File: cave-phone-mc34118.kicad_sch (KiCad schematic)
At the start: 53 parts

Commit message: v0.1 (wrong U2 package)
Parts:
- removed SW?: SW_SPST, symbol Switch:SW_SPST
- added BT1: 18650, Battery:BatteryHolder_MPD_BH-18650-PC2, symbol Device:Battery_Cell
- added C1: 4,7µF, Capacitor_Tantalum_SMD:CP_EIA-3528-21_Kemet-B, symbol Device:C_Polarized
- added C12: 150pF, Capacitor_SMD:C_0603_1608Metric, symbol Device:C
- added C16: 20µF, Capacitor_Tantalum_SMD:CP_EIA-3528-21_Kemet-B, symbol Device:C_Polarized
- added C29: 1000µF, Capacitor_SMD:CP_Elec_10x10.5, symbol Device:C_Polarized
- added D1: BAT760.115, Diode_SMD:D_SOD-323, symbol Device:D_Schottky
- added D2: DB107GS, Diode_SMD:Diode_Bridge_Vishay_DFS, symbol Device:D_Bridge_+-AA
- added D3: BZV55C5V1, Diode_SMD:D_MiniMELF, symbol Diode:BZV55C5V1
- added D4: PESD5V0L1BA, Diode_SMD:D_SOD-323, symbol cave-phone:PESD5V0L1BA
- added D5: LED, LED_THT:LED_D3.0mm, symbol Device:LED
- added E1: 2051-09-SM-RPLF (90V), Fuse:Fuse_1812_4532Metric, symbol Device:SparkGap
- added J1: Conn_01x02_Female, Connector_Molex:Molex_SPOX_5267-02A_1x02_P2.50mm_Vertical, symbol Connector:Conn_01x02_Female
- added L1: 1,8µH, Inductor_SMD:L_1008_2520Metric, symbol Device:L
- added R23: 5K, Resistor_SMD:R_0603_1608Metric, symbol Device:R
- added R8: 29,4K, Resistor_SMD:R_0603_1608Metric, symbol Device:R
- added R9: 10K, Resistor_SMD:R_0603_1608Metric, symbol Device:R
- added SW1: L-KLS7-SK02-12E12-EG7, cave-phone:KLS7-SK02-12E12, symbol Switch:SW_SPDT
- added SW3: SW_SPST, Connector_PinHeader_2.54mm:PinHeader_1x02_P2.54mm_Vertical, symbol Switch:SW_SPST
- added U1: LT1935, Package_TO_SOT_SMD:SOT-23-5, symbol cave-phone:LT1935
- C10, C11, C13, C14, C15, C17, C18, C19, C20, C21, C22, C23, C24, C26, C27, C28, C4, C6, C7, C9: renamed from C?; footprint (none) -> Capacitor_SMD:C_0603_1608Metric
- C2, C25, C8: renamed from C?; footprint (none) -> Capacitor_Tantalum_SMD:CP_EIA-3528-21_Kemet-B
- C3: renamed from C?; footprint (none) -> Capacitor_Tantalum_SMD:CP_EIA-3528-21_Kemet-B; symbol Device:C -> Device:C_Polarized
- C5: renamed from C?; footprint (none) -> Capacitor_SMD:C_0805_2012Metric
- LS1: renamed from LS?; footprint (none) -> Connector_Molex:Molex_SPOX_5267-02A_1x02_P2.50mm_Vertical
- MK1: renamed from MK?; footprint (none) -> snapeda-mic:MIC_CMA-4544PF-W
- R1, R10, R11, R12, R13, R14, R15, R16, R17, R18, R19, R2, R20, R21, R22, R3, R4, R5, R6, R7: renamed from R?; footprint (none) -> Resistor_SMD:R_0603_1608Metric
- RV1: renamed from RV?; footprint (none) -> Potentiometer_THT:Potentiometer_Alps_RK163_Single_Horizontal
- SW2: renamed from SW?; footprint (none) -> Button_Switch_SMD:SW_Push_1P1T_NO_6x6mm_H9.5mm
- T1: renamed from T?; value Transformer_1P_1S -> SM-LP-5001; footprint (none) -> cave-phone:SM-LP-5001
- U2: renamed from U?; footprint Package_SO:SSOP-28_5.3x10.2mm_P0.65mm -> Package_SO:SOIC-28W_7.5x17.9mm_P1.27mm
- U3: renamed from U?; value MC34119P -> MC34119G-SO8; footprint Package_DIP:DIP-8_W7.62mm -> Package_SO:SOP-8_3.9x4.9mm_P1.27mm; symbol cave-phone:MC34119P -> cave-phone:MC34119G-S08-R
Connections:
- net GND: now also C3.2, U2.3 (CD), U3.1 (CD), BT1.2 (-), C1.2, C16.2, C29.2, D2.2 (-), D3.2 (A), R23.2, R9.2, U1.2 (GND); no longer C3.1
- net VCC: now also C12.2, C16.1, C29.1, D1.1 (K), D2.1 (+), D3.1 (K), D5.2 (A), R8.1
- net at R1.2, U2.14 (CT): now also C3.1; no longer C3.2
- net at T1.3 (SA): now also D2.4, SW3.1 (A)
- net at T1.4 (SB): now also D4.2 (A), E1.2, J1.1 (Pin_1)
- new net: C1.1, L1.1, SW1.3 (C), U1.4 (EN), U1.5 (VIN)
- new net: D1.2 (A), L1.2, U1.1 (SW)
- new net: D2.3, D4.1 (K1), E1.1, J1.2 (Pin_2), SW3.2 (B)
- new net: BT1.1 (+), SW1.2 (B)
- new net: C12.1, R8.2, R9.1, U1.3 (FB)
- new net: D5.1 (K), R23.1
- no-connect marks 0 -> 1
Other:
- note added: "1. Рассмотреть LM27313 в качестве импульсного преобразователя. 2. Добавить защиту от переразряда 3. Проработать схему питания от центральной батареи (ограничительный резистор, пропускание переменной составляющей мимо диодного моста)"
- note added: "Connector MX-5267-02A"
- note added: "Line"
- note added: "RV1 - R16148-1A-2-A22K"
- note removed: "Enable"

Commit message: Fix prototype status
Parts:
- added R?: 20K, Resistor_SMD:R_0603_1608Metric, symbol Device:R
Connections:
- net GND: now also SW2.1 (A)
- net VB: now also RV1.1; no longer RV1.3
- net VCC: now also C8.1, R?.2; no longer C8.2, SW2.1 (A)
- net at R5.2, U2.16 (CPT): now also C8.2; no longer C8.1
- net at SW2.2 (B), U2.12 (MUT): now also R?.1
- net at R15.2: now also RV1.3; no longer RV1.1
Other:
- note added: "Push to talk"
- note removed: "Mute"
- moved on the sheet: C8, RV1
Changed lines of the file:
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@@
   (junction (at 148.59 35.56) (diameter 0) (color 0 0 0 0)
+  )
+  (junction (at 83.82 40.64) (diameter 0) (color 0 0 0 0)
   )
   (junction (at 220.98 46.99) (diameter 0) (color 0 0 0 0)
@@
     (stroke (width 0) (type default) (color 0 0 0 0))
   )
-  (wire (pts (xy 82.55 40.64) (xy 97.79 40.64))
+  (wire (pts (xy 82.55 40.64) (xy 83.82 40.64))
     (stroke (width 0) (type default) (color 0 0 0 0))
   )
@@
     (stroke (width 0) (type default) (color 0 0 0 0))
   )
+  (wire (pts (xy 83.82 29.21) (xy 83.82 30.48))
+    (stroke (width 0) (type default) (color 0 0 0 0))
+  )
   (wire (pts (xy 88.9 34.29) (xy 88.9 55.88))
     (stroke (width 0) (type default) (color 0 0 0 0))
@@
     (stroke (width 0) (type default) (color 0 0 0 0))
   )
-  (wire (pts (xy 69.85 38.1) (xy 69.85 40.64))
-    (stroke (width 0) (type default) (color 0 0 0 0))
-  )
   (wire (pts (xy 74.93 86.36) (xy 78.74 86.36))
     (stroke (width 0) (type default) (color 0 0 0 0))
@@
     (stroke (width 0) (type default) (color 0 0 0 0))
   )
+  (wire (pts (xy 83.82 40.64) (xy 97.79 40.64))
+    (stroke (width 0) (type default) (color 0 0 0 0))
+  )
   (wire (pts (xy 71.12 182.88) (xy 50.8 182.88))
     (stroke (width 0) (type default) (color 0 0 0 0))
@@
   )
   (wire (pts (xy 62.23 39.37) (xy 62.23 40.64))
+    (stroke (width 0) (type default) (color 0 0 0 0))
+  )
+  (wire (pts (xy 83.82 38.1) (xy 83.82 40.64))
     (stroke (width 0) (type default) (color 0 0 0 0))
   )
@@
   )
   (text "1. Рассмотреть LM27313 в качестве импульсного преобразователя.\n2. Добавить защиту от переразряда\n3. Проработать схему питания от центральной батареи (ограничительный резистор, пропускание переменной составляющей мимо диодного моста)"
-    (at 207.01 148.59 0)
+    (at 152.4 162.56 0)
     (effects (font (size 1.27 1.27)) (justify left bottom))
   )
-  (text "Mute" (at 76.2 44.45 0)
+  (text "Push to talk" (at 73.66 44.45 0)
     (effects (font (size 1.27 1.27)) (justify left bottom))
   )
@@
     (pin "2")
   )
-  (symbol (lib_id "Device:C_Polarized") (at 80.01 76.2 270) (unit 1)
+  (symbol (lib_id "Device:C_Polarized") (at 80.01 76.2 90) (mirror x) (unit 1)
     (in_bom yes) (on_board yes)
-    (property "Reference" "C8" (id 0) (at 74.93 72.39 90))
-    (property "Value" "47µF" (id 1) (at 74.93 74.93 90))
-    (property "Footprint" "Capacitor_Tantalum_SMD:CP_EIA-3528-21_Kemet-B" (id 2) (at 76.2 77.1652 0)
+    (property "Reference" "C8" (id 0) (at 85.09 72.39 90))
+    (property "Value" "47µF" (id 1) (at 85.09 74.93 90))
+    (property "Footprint" "Capacitor_Tantalum_SMD:CP_EIA-3528-21_Kemet-B" (id 2) (at 83.82 77.1652 0)
       (effects (font (size 1.27 1.27)) hide)
     )
     (property "Datasheet" "~" (id 3) (at 80.01 76.2 0)
+      (effects (font (size 1.27 1.27)) hide)
+    )
+    (pin "1")
+    (pin "2")
+  )
+  (symbol (lib_id "Device:R") (at 83.82 34.29 180) (unit 1)
+    (in_bom yes) (on_board yes)
+    (property "Reference" "R?" (id 0) (at 78.74 28.9749 0)
+      (effects (font (size 1.27 1.27)) (justify right))
+    )
+    (property "Value" "20K" (id 1) (at 78.74 31.75 0)
+      (effects (font (size 1.27 1.27)) (justify right))
+    )
+    (property "Footprint" "Resistor_SMD:R_0603_1608Metric" (id 2) (at 85.598 34.29 90)
+      (effects (font (size 1.27 1.27)) hide)
+    )
+    (property "Datasheet" "~" (id 3) (at 83.82 34.29 0)
       (effects (font (size 1.27 1.27)) hide)
     )
@@
     (pin "8")
   )
-  (symbol (lib_id "Device:R_Potentiometer") (at 135.89 110.49 90) (unit 1)
+  (symbol (lib_id "Device:R_Potentiometer") (at 135.89 110.49 270) (mirror x) (unit 1)
     (in_bom yes) (on_board yes)
-    (property "Reference" "RV1" (id 0) (at 139.7 113.03 90))
-    (property "Value" "20K" (id 1) (at 139.7 115.57 90))
+    (property "Reference" "RV1" (id 0) (at 139.7 105.41 90))
+    (property "Value" "20K" (id 1) (at 139.7 107.95 90))
     (property "Footprint" "Potentiometer_THT:Potentiometer_Alps_RK163_Single_Horizontal" (id 2) (at 135.89 110.49 0)
       (effects (font (size 1.27 1.27)) hide)
@@
     (pin "2")
   )
-  (symbol (lib_id "power:VCC") (at 69.85 38.1 0) (unit 1)
-    (in_bom yes) (on_board yes) (fields_autoplaced)
-    (property "Reference" "#PWR07" (id 0) (at 69.85 41.91 0)
-      (effects (font (size 1.27 1.27)) hide)
-    )
-    (property "Value" "VCC" (id 1) (at 69.85 34.4955 0))
-    (property "Footprint" "" (id 2) (at 69.85 38.1 0)
-      (effects (font (size 1.27 1.27)) hide)
-    )
-    (property "Datasheet" "" (id 3) (at 69.85 38.1 0)
-      (effects (font (size 1.27 1.27)) hide)
-    )
-    (pin "1")
-  )
   (symbol (lib_id "power:VCC") (at 62.23 30.48 0) (unit 1)
     (in_bom yes) (on_board yes) (fields_autoplaced)
@@
     (pin "1")
     (pin "2")
+  )
+  (symbol (lib_id "power:GND") (at 69.85 40.64 0) (unit 1)
+    (in_bom yes) (on_board yes) (fields_autoplaced)
+    (property "Reference" "#PWR?" (id 0) (at 69.85 46.99 0)
+      (effects (font (size 1.27 1.27)) hide)
+    )
+    (property "Value" "GND" (id 1) (at 69.85 45.2025 0))
+    (property "Footprint" "" (id 2) (at 69.85 40.64 0)
+      (effects (font (size 1.27 1.27)) hide)
+    )
+    (property "Datasheet" "" (id 3) (at 69.85 40.64 0)
+      (effects (font (size 1.27 1.27)) hide)
+    )
+    (pin "1")
   )
   (symbol (lib_id "Device:C_Polarized") (at 62.23 99.06 0) (unit 1)
@@
     )
     (property "Datasheet" "" (id 3) (at 72.39 67.31 0)
+      (effects (font (size 1.27 1.27)) hide)
+    )
+    (pin "1")
+  )
+  (symbol (lib_id "power:VCC") (at 83.82 29.21 0) (unit 1)
+    (in_bom yes) (on_board yes) (fields_autoplaced)
+    (property "Reference" "#PWR?" (id 0) (at 83.82 33.02 0)
+      (effects (font (size 1.27 1.27)) hide)
+    )
+    (property "Value" "VCC" (id 1) (at 83.82 25.6055 0))
+    (property "Footprint" "" (id 2) (at 83.82 29.21 0)
+      (effects (font (size 1.27 1.27)) hide)
+    )
+    (property "Datasheet" "" (id 3) (at 83.82 29.21 0)
       (effects (font (size 1.27 1.27)) hide)
     )
@@
       (reference "#PWR06") (unit 1) (value "VB") (footprint "")
     )
-    (path "/656d4118-0bfe-4834-85c1-42a3cf39a8d3"
-      (reference "#PWR07") (unit 1) (value "VCC") (footprint "")
-    )
     (path "/a5ce506c-f597-49c1-be5f-e198c10d518a"
       (reference "#PWR08") (unit 1) (value "VCC") (footprint "")
@@
       (reference "#PWR025") (unit 1) (value "VCC") (footprint "")
     )
+    (path "/8b4d6a36-8b8a-47fa-9b34-e1f16ae22191"
+      (reference "#PWR?") (unit 1) (value "GND") (footprint "")
+    )
+    (path "/ac486a53-e328-4f5b-afe1-0757728cd402"
+      (reference "#PWR?") (unit 1) (value "VCC") (footprint "")
+    )
     (path "/eaba4031-3b8f-408d-8784-adcaa5d858b2"
       (reference "BT1") (unit 1) (value "18650") (footprint "Battery:BatteryHolder_MPD_BH-18650-PC2")
@@
       (reference "R23") (unit 1) (value "5K") (footprint "Resistor_SMD:R_0603_1608Metric")
     )
+    (path "/01fd0491-9c79-48df-9cb9-c77a3408e52e"
+      (reference "R?") (unit 1) (value "20K") (footprint "Resistor_SMD:R_0603_1608Metric")
+    )
     (path "/1abb2b04-421f-4dfa-846c-5a6998a6e226"

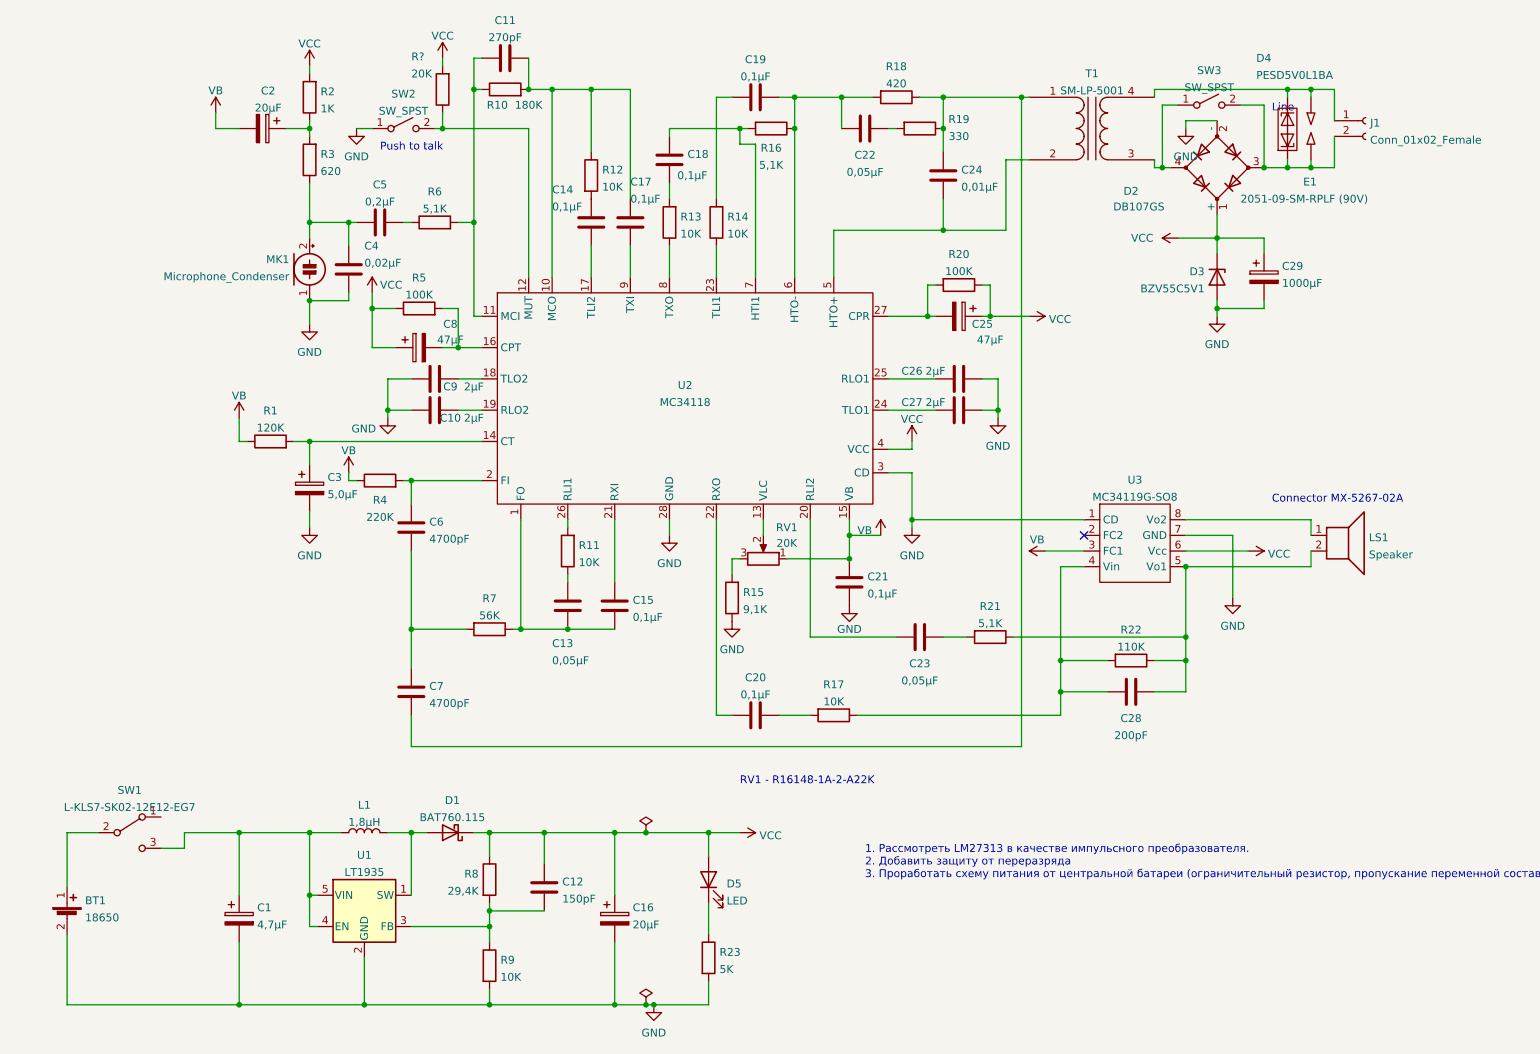
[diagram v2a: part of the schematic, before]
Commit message: sch: Remove DC-DC
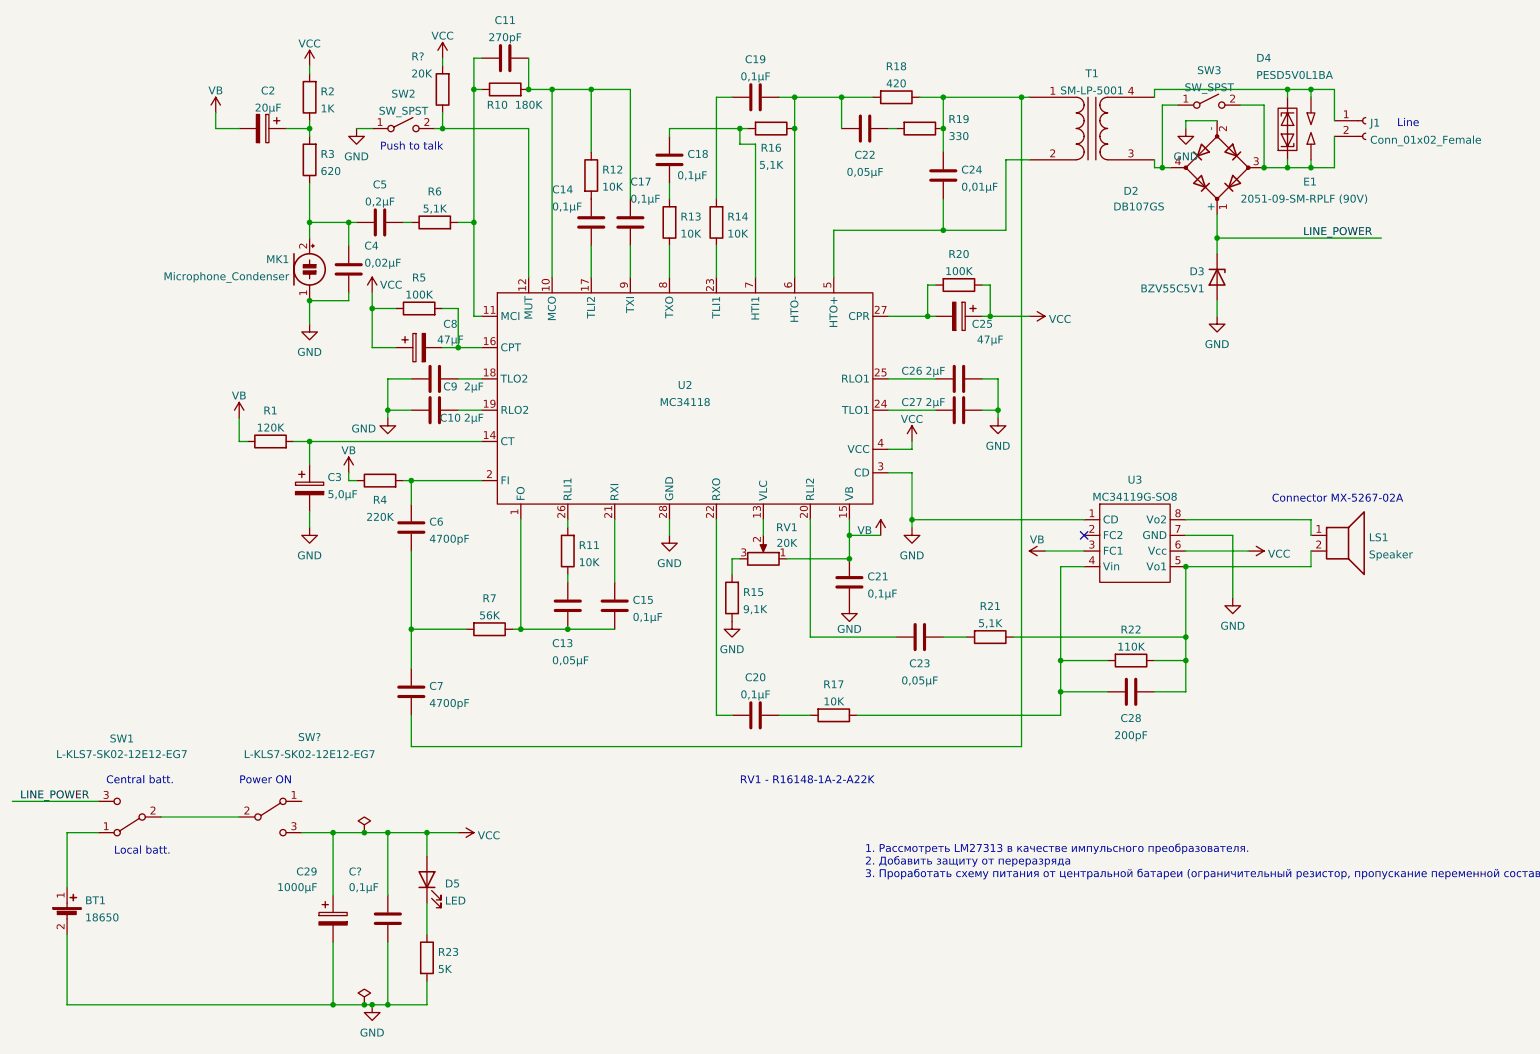
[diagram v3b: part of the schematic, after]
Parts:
- removed C1: 4,7µF, Capacitor_Tantalum_SMD:CP_EIA-3528-21_Kemet-B, symbol Device:C_Polarized
- removed C12: 150pF, Capacitor_SMD:C_0603_1608Metric, symbol Device:C
- removed C16: 20µF, Capacitor_Tantalum_SMD:CP_EIA-3528-21_Kemet-B, symbol Device:C_Polarized
- removed D1: BAT760.115, Diode_SMD:D_SOD-323, symbol Device:D_Schottky
- removed L1: 1,8µH, Inductor_SMD:L_1008_2520Metric, symbol Device:L
- removed R8: 29,4K, Resistor_SMD:R_0603_1608Metric, symbol Device:R
- removed R9: 10K, Resistor_SMD:R_0603_1608Metric, symbol Device:R
- removed U1: LT1935, Package_TO_SOT_SMD:SOT-23-5, symbol cave-phone:LT1935
- added C?: 0,1µF, Capacitor_SMD:C_0603_1608Metric, symbol Device:C
- added SW?: L-KLS7-SK02-12E12-EG7, cave-phone:KLS7-SK02-12E12, symbol Switch:SW_SPDT
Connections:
- net GND: now also C?.2
- net VCC: now also C?.1, SW?.3 (C); no longer D2.1 (+), D3.1 (K)
- net LINE_POWER: now reaches SW1.3 (C)
- net LINE_POWER: now also D2.1 (+), D3.1 (K)
- net at SW1.1 (A): now also BT1.1 (+)
- net at SW1.2 (B): now also SW?.2 (B); no longer BT1.1 (+)
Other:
- note added: "Central batt."
- note added: "Local batt."
- note added: "Power ON"
- moved on the sheet: C29, D5, R23, SW1

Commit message: Fix some errors and add improvements
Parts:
- removed C21: 0,1µF, Capacitor_SMD:C_0603_1608Metric, symbol Device:C
- removed SW3: SW_SPST, Connector_PinHeader_2.54mm:PinHeader_1x02_P2.54mm_Vertical, symbol Switch:SW_SPST
- added C12: 0,1µF, Capacitor_SMD:C_0603_1608Metric, symbol Device:C
- added C21: (no value), Capacitor_Tantalum_SMD:CP_EIA-3528-21_Kemet-B, symbol Device:C_Polarized
- added R9: (no value), Resistor_SMD:R_0603_1608Metric, symbol Device:R
- added SW4: SW_SPST, Button_Switch_SMD:SW_Push_1P1T_NO_6x6mm_H9.5mm, symbol Switch:SW_SPST
- R12, R14: value 10K -> (none)
- R16: value 5,1K -> (none)
- R18: value 420 -> (none)
- R19: value 330 -> (none)
- gave numbers to parts that had none: 3
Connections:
- net GND: now also C21.2
- net VB: now also C21.1
- net at C24.2, T1.2 (AB), U2.5 (HTO+): now also SW4.2 (B)
- net at D2.4, T1.3 (SA): now also C12.2
- net at D2.3, D4.1 (K1), E1.1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: now also C12.1
- net at C18.1, R13.2: now also R9.2
- new net: R9.1, SW4.1 (A)
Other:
- note added: "1. Добавить защиту от переразряда 2. Проработать схему питания от центральной батареи (ограничительный резистор, пропускание переменной составляющей мимо диодного моста)"
- note added: "Call"
- note added: "Hybrid A. Gain = -R16/R13"
- note added: "Place near the pin 4 of MC34118"
- note added: "История: 1. Перевернули RV1 2. Что-то было не то с какими-то конденсаторами (неполярный вместо полярного, кажется, и полярность одного из была неверна) :) 3. Удалён DC/DC конвертер 4. Добавлен переключатель ЦБ/МБ 5. Исправлено ошибочное значение R16 (было 5.1К из китайского даташита вместо 51К из мотороловского) 6. Кнопка Mute заменена кнопкой Push-To-Talk 7. Номинал R14 изменён с 10К на 5,1К (ош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"
- note removed: "1. Рассмотреть LM27313 в качестве импульсного преобразователя. 2. Добавить защиту от переразряда 3. Проработать схему питания от центральной батареи (ограничительный резистор, пропускание переменной составляющей мимо диодного моста)"
